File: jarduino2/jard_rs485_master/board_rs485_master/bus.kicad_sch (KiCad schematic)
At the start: 19 parts, among them J3 POWER_OYAS_12V, J4 BUS_OYAS, Q1 BPC_2N2222A, Q2 BPC_IPP034N03L, U4 BPC_Mod485

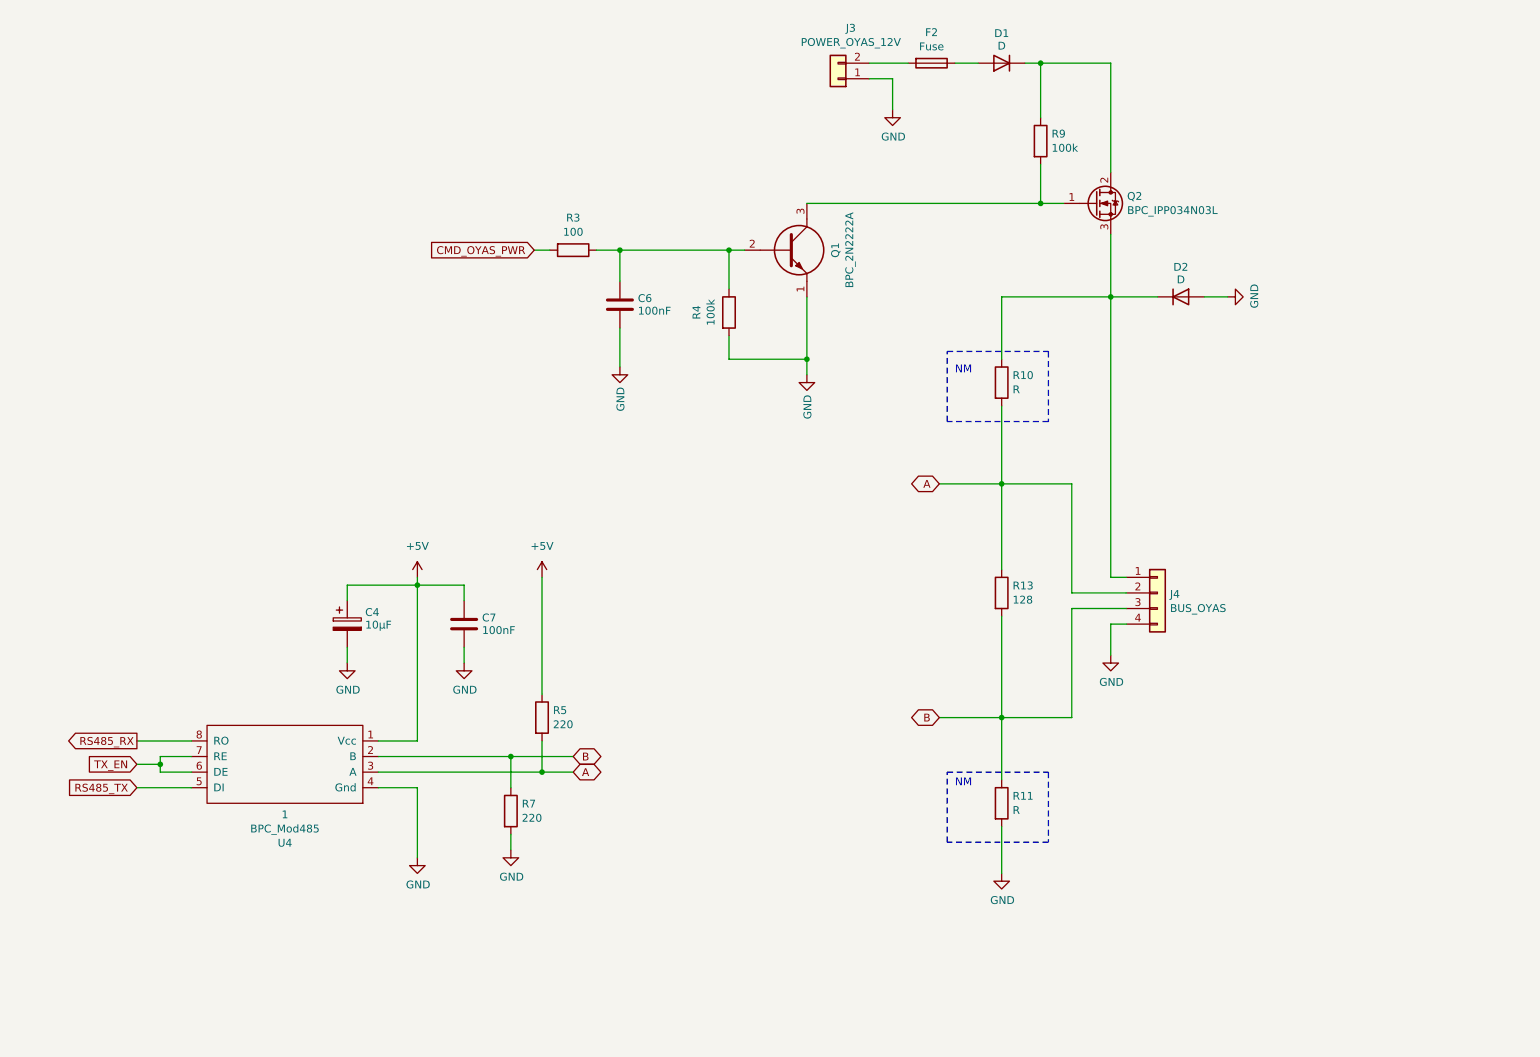
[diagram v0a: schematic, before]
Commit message: Candidate pour revue du master Oyas (avec modules en tant que shield MEGA)
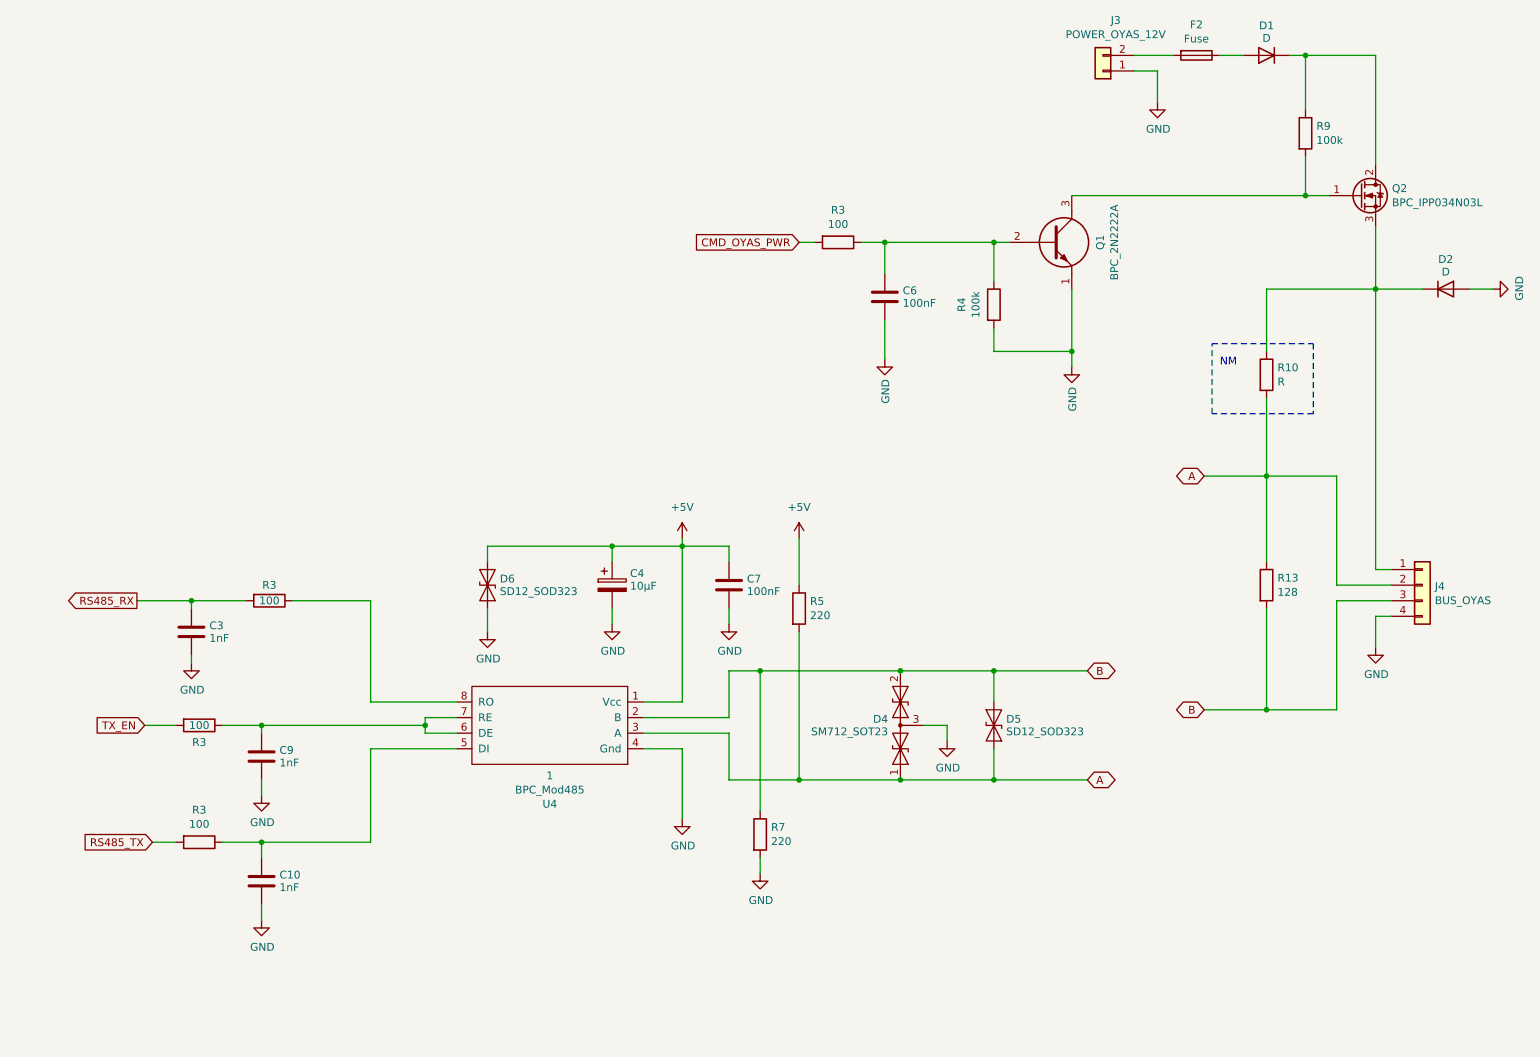
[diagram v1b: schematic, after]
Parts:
- removed R11: R, Resistor_THT:R_Axial_DIN0204_L3.6mm_D1.6mm_P7.62mm_Horizontal, symbol Device:R
- added C10, C3, C9: 1nF, Capacitor_THT:C_Disc_D5.0mm_W2.5mm_P2.50mm, symbol Device:C
- added D4: SM712_SOT23, Package_TO_SOT_SMD:SOT-23, symbol Diode:SM712_SOT23
- added D5, D6: SD12_SOD323, Diode_SMD:D_SOD-323, symbol Diode:SD12_SOD323
- added R3 (x3): 100, Resistor_THT:R_Axial_DIN0204_L3.6mm_D1.6mm_P7.62mm_Horizontal, symbol Device:R
- D1: footprint Diode_THT:D_A-405_P2.54mm_Vertical_AnodeUp -> Diode_THT:D_A-405_P12.70mm_Horizontal
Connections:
- net +5V: now also D6.2 (A2)
- net A: now also D4.1 (A1), D5.1 (A1)
- net B: now also D4.2 (A2), D5.2 (A2)
- net GND: now also C10.2, C3.2, C9.2, D4.3 (common), D6.1 (A1)
- net RS485_RX: now also C3.1, R3.2; no longer U4.8 (RO)
- net RS485_TX: now also R3.2; no longer U4.5 (DI)
- net TX_EN: now also R3.2; no longer U4.6 (DE), U4.7 (RE)
- new net: C10.1, R3.1, U4.5 (DI)
- new net: C9.1, R3.1, U4.6 (DE), U4.7 (RE)
- new net: R3.1, U4.8 (RO)
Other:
- company: (none) -> BPC
- title: (none) -> Commande des OYA - Maître RS485
- moved on the sheet: C4, C6, C7, D1, D2, F2, J3, J4, Q1, Q2, R10, R13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

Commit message: Finalisation dossier
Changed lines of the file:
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@@
   (title_block
     (title "Commande des OYA - Maître RS485")
-    (date "2024-03-30")
+    (date "2024-03-31")
     (rev "A0")
     (company "BPC")
@@
   (symbol (lib_id "Device:R") (at 59.69 113.03 270) (unit 1)
     (in_bom yes) (on_board yes) (dnp no)
-    (property "Reference" "R3" (at 59.69 110.49 90)
+    (property "Reference" "R3" (at 59.69 115.57 90)
       (effects (font (size 1.27 1.27)))
     )
@@
   (symbol (lib_id "Device:R") (at 48.26 152.4 270) (unit 1)
     (in_bom yes) (on_board yes) (dnp no)
-    (property "Reference" "R3" (at 48.26 147.1422 90)
-      (effects (font (size 1.27 1.27)))
-    )
-    (property "Value" "100" (at 48.26 149.4536 90)
-      (effects (font (size 1.27 1.27)))
-    )
+    (property "Reference" "R3" (at 48.26 154.94 90)
+      (effects (font (size 1.27 1.27)))
+    )
+    (property "Value" "100" (at 48.26 152.4 90)
+      (effects (font (size 1.27 1.27)))
+    )

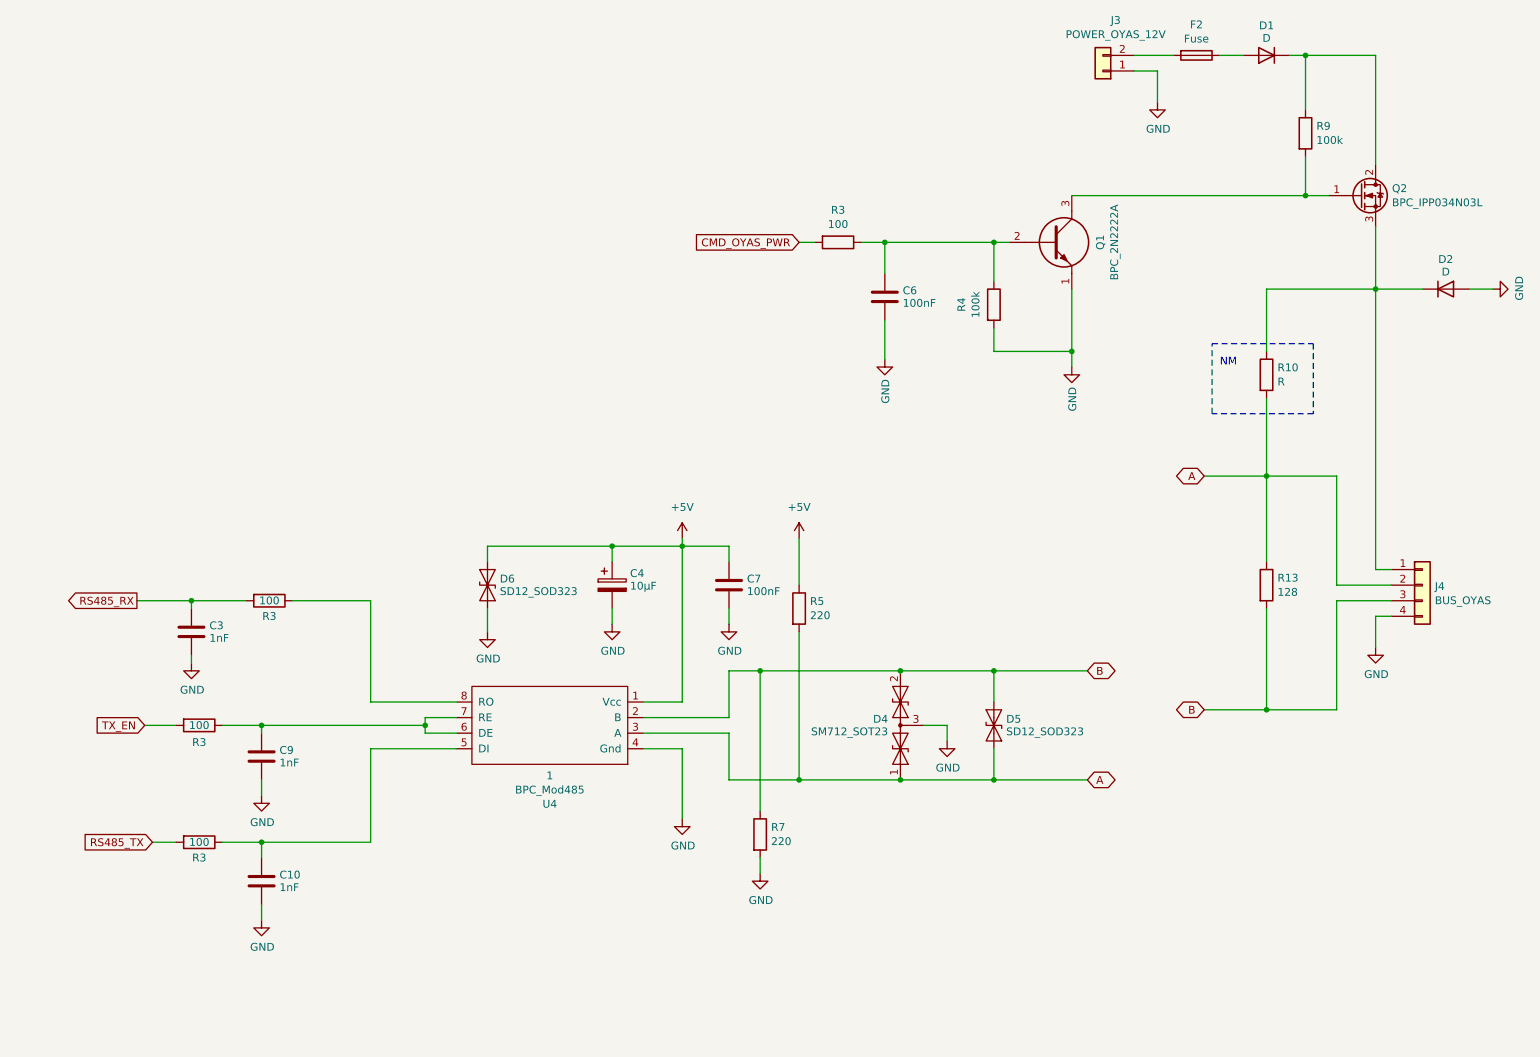
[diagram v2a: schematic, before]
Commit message: Amélioration suite remise en route:
  - Agrandissement trous des LEDs D1 et D3
  - Correction erreur type du MOS P GDS
  - Agrandissement empreintes de R5,R7,R13 et R10 + verticales
  - Ajout de la description des opérations de rework pour le MOD485
  - Ajout d'une interface pour adapter le bus (5V, A, B et Gnd)
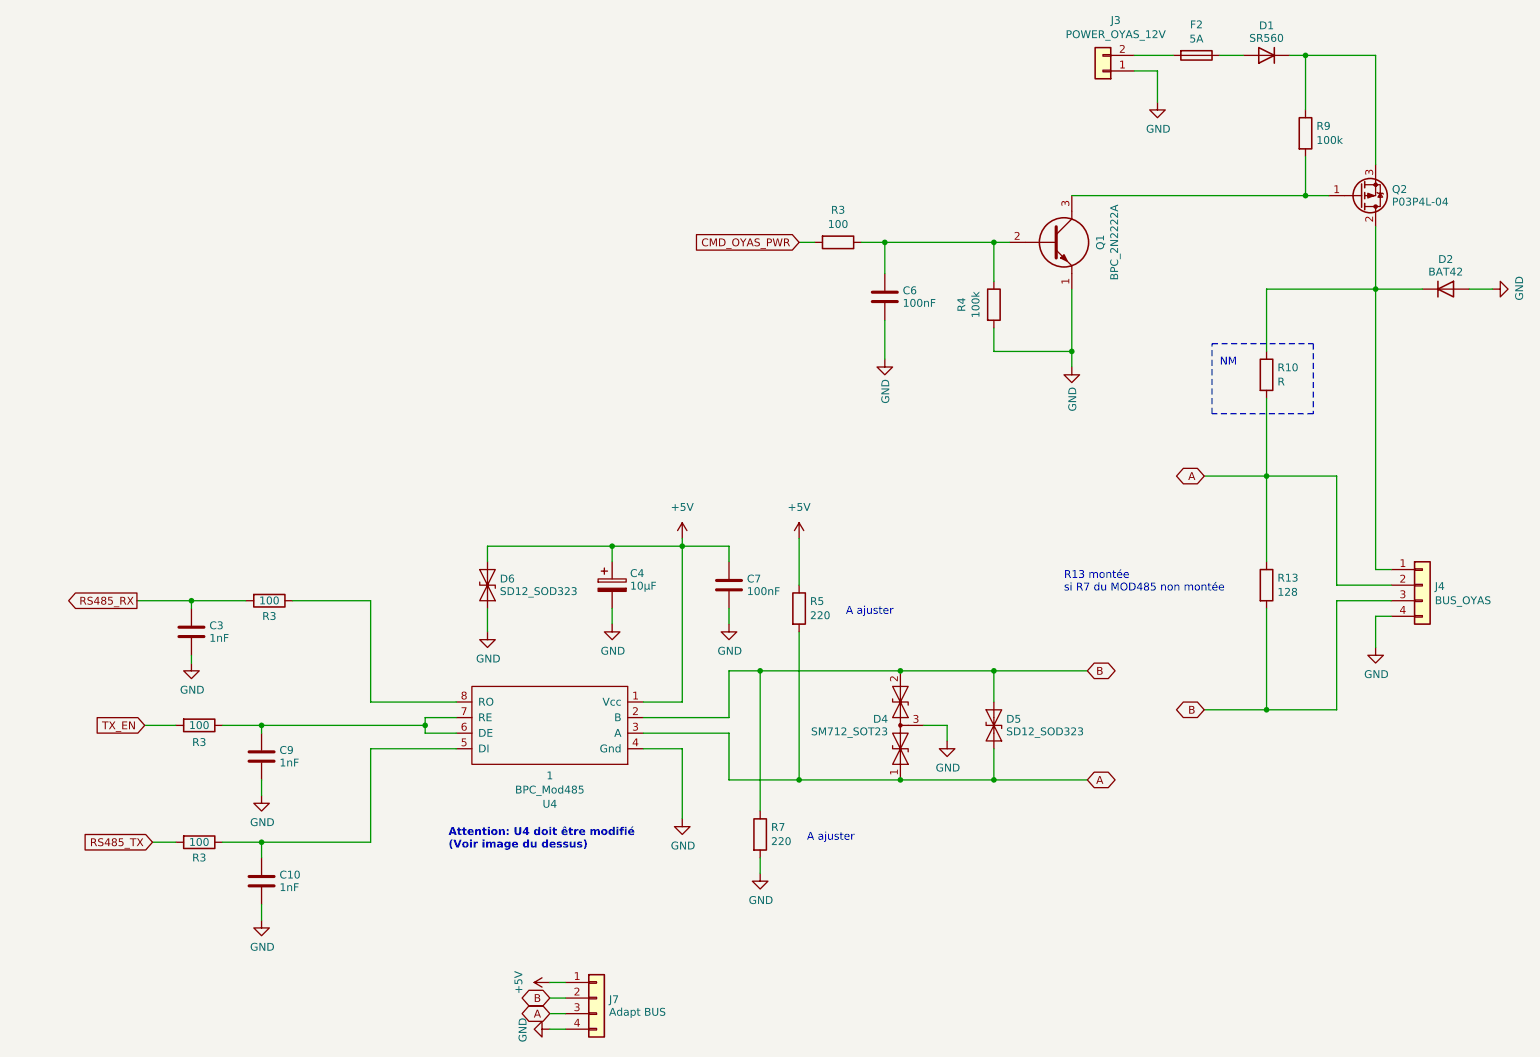
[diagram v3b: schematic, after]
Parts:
- removed Q2: BPC_IPP034N03L, Package_TO_SOT_THT:TO-220-3_Vertical, symbol bpc:BPC_IPP034N03L
- added J7: Adapt BUS, Connector_PinHeader_2.54mm:PinHeader_1x04_P2.54mm_Vertical, symbol Connector_Generic:Conn_01x04
- added Q2: P03P4L-04, Package_TO_SOT_THT:TO-220-3_Vertical, symbol bpc:P03P4L-04
- D1: value D -> SR560; footprint Diode_THT:D_A-405_P12.70mm_Horizontal -> Diode_THT:D_DO-15_P12.70mm_Horizontal
- D2: value D -> BAT42
- F2: value Fuse -> 5A
- R10, R13, R5, R7: footprint Resistor_THT:R_Axial_DIN0204_L3.6mm_D1.6mm_P7.62mm_Horizontal -> Resistor_THT:R_Axial_DIN0414_L11.9mm_D4.5mm_P5.08mm_Vertical
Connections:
- net +5V: now also J7.1 (Pin_1)
- net A: now also J7.3 (Pin_3)
- net B: now also J7.2 (Pin_2)
- net GND: now also J7.4 (Pin_4)
- net at D1.1 (K), R9.1: now also Q2.3 (S)
- net at Q1.3, R9.2: now also Q2.1 (G)
- net at D2.1 (K), J4.1 (Pin_1), R10.1: now also Q2.2 (D)
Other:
- note added: "A ajuster"
- note added: "Attention: U4 doit être modifié (Voir image du dessus)"
- note added: "R13 montée si R7 du MOD485 non montée"

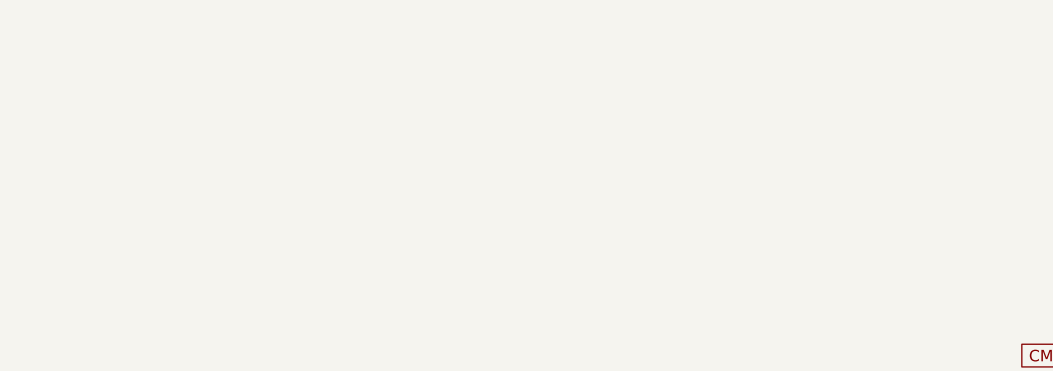
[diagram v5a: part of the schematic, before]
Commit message: Titres + finitions (vias)
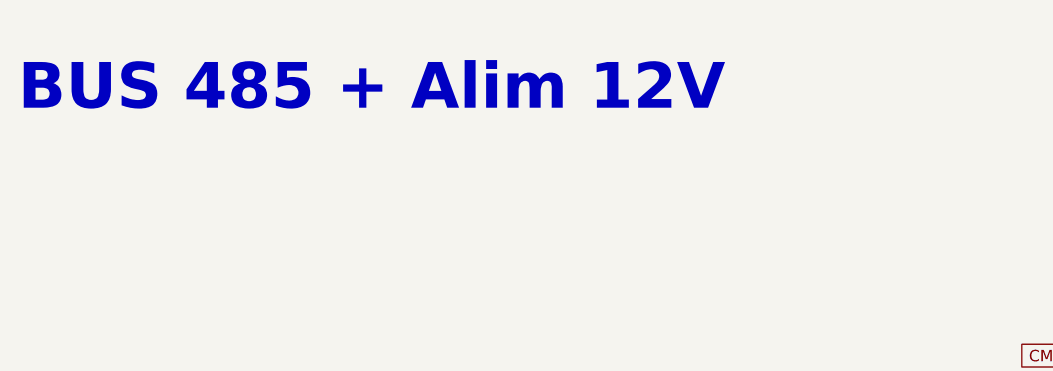
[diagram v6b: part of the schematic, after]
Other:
- note added: "BUS 485 + Alim 12V"
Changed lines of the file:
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@@
     (effects (font (size 1.27 1.27)) (justify left bottom))
+  )
+  (text "BUS 485 + Alim 12V" (at 17.78 27.94 0)
+    (effects (font (size 5.08 5.08) (thickness 2.54) bold) (justify left bottom))
   )
   (text "A ajuster" (at 147.32 152.4 0)

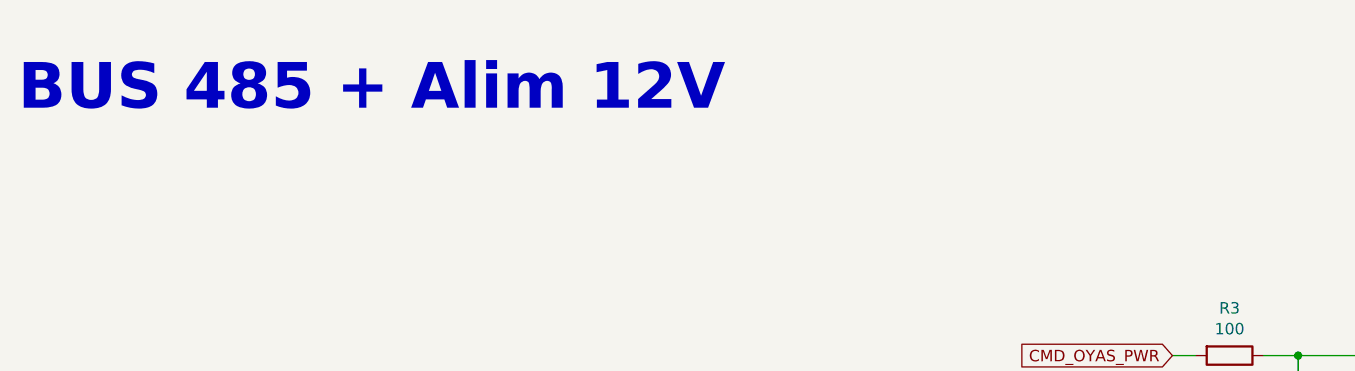
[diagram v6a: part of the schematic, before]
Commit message: Réaffactation des commandes PWR de Wifi et LEDs (compatibilité soft) + suppression de la sheet Wifi sur le schéma (regreoupé dans UC)
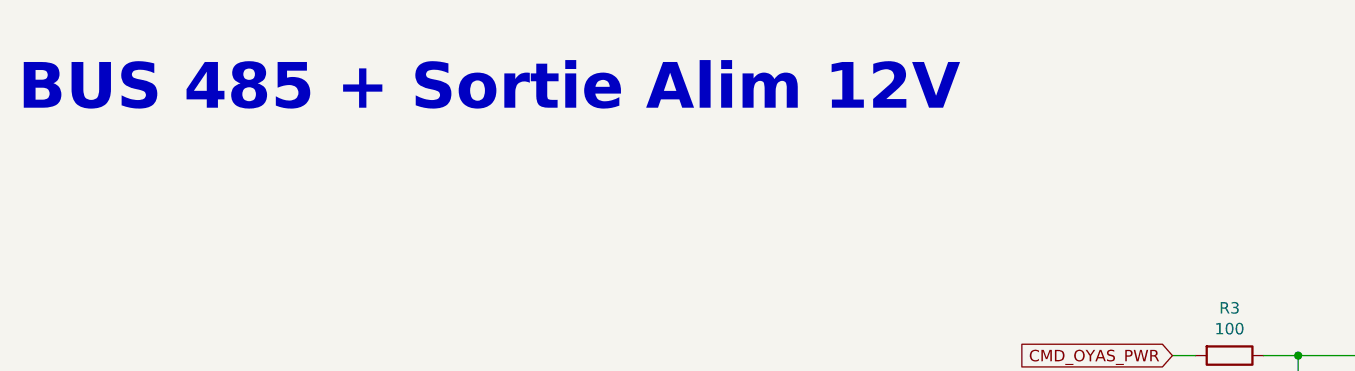
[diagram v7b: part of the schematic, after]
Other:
- note added: "BUS 485 + Sortie Alim 12V"
- note removed: "BUS 485 + Alim 12V"
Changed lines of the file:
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@@
   (title_block
     (title "Commande des OYA - Maître RS485")
-    (date "2024-04-26")
+    (date "2024-05-06")
     (rev "B0")
     (company "BPC")
@@
     (effects (font (size 1.27 1.27)) (justify left bottom))
   )
-  (text "BUS 485 + Alim 12V" (at 17.78 27.94 0)
+  (text "BUS 485 + Sortie Alim 12V" (at 17.78 27.94 0)
     (effects (font (size 5.08 5.08) (thickness 2.54) bold) (justify left bottom))
   )
